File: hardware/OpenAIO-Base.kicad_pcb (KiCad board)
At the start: 8 copper layers, 35 x 35 mm, 264 parts, among them J15 5V, J16 5V, J17 GND, J18 GND, J20 LED, J21 LED, J24 5V, J25 5V, J27 GND, J28 GND, J29 BUZ-, J31 LED, J32 LED, J33 BUZ+, J41 10V, J51 GND, J90 OpenAIO-Core PCBA (consigned), Q10 DOY180N03T, Q11 DOY180N03T, Q12 DOY180N03T, Q13 DOY180N03T, Q14 DOY180N03T, Q15 DOY180N03T, Q16 DOY180N03T, Q17 DOY180N03T, Q18 DOY180N03T, Q19 DOY180N03T, Q20 DOY180N03T, Q21 DOY180N03T, Q22 DOY180N03T, Q23 DOY180N03T, Q24 DOY180N03T, Q25 DOY180N03T, Q26 DOY180N03T, Q3 DOY180N03T, Q4 DOY180N03T, Q5 DOY180N03T, Q6 DOY180N03T, Q7 DOY180N03T, Q8 DOY180N03T, Q9 DOY180N03T, U12 SM06B-SRSS-TB(LF)(SN), U13 AT32F421G8U7, U14 NSG2065Q, U15 AT32F421G8U7, U16 NSG2065Q, U17 AT32F421G8U7, U18 NSG2065Q, U19 AT32F421G8U7, U20 NSG2065Q, U21 SX1281IMLTRT, U22 ESP32-C3FH4, U23 TLV75533PDQNR, U24 AIO_outline, U25 INA186A3IDCKR, U27 TLV75533PDQNR, U3 LMR51430YFDDCR, U4 LMR51430YFDDCR, X2 CJ17-400001010B20

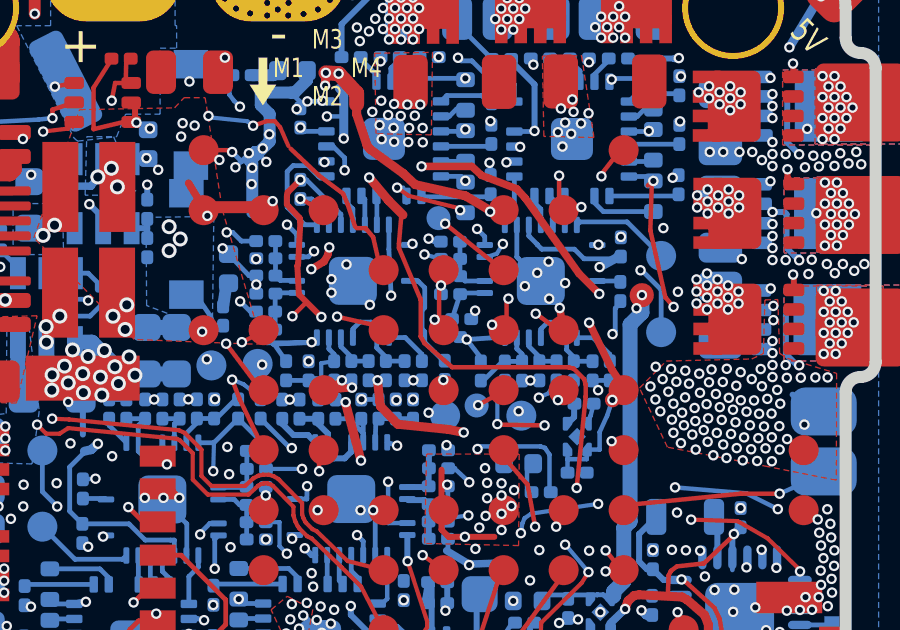
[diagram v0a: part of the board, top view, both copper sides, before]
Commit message: Base: revert the FB8e J90.14 GND via, R107 back to (78.73, 58.53) (FB7 step 4)
FB8e moved R107 (ESC4 phase-B divider) 0.37 mm east to make room for a
J90.14 GND via. That put R107.1 (/4B, the motor phase node) 0.045 mm from
the U19 QFN-28 body, beside U19's pin-8 terminal, which has no land: a
solder bridge there puts the phase voltage on the ESC4 MCU. The FB8e
classifier compared body-body and land-land only and missed the
land-to-body gap; the courtyard check found it. No other site for that via
(PB4 track, R105/R106 column, U19), so J90.14 goes back to its shared F
track via (78.41, 57.41). Geometry in the box equals b27fb75.
DRC 0 errors, unconnected 0, parity 70, +BATT 0.585 GND 0.357 mOhm,
+5V 56.4 mV.

Co-Authored-By: Claude Opus 5.5 <noreply@anthropic.com>
Claude-Session: https://claude.ai/code/session_01KTp3FLjVXfXdWrkmr6af7d
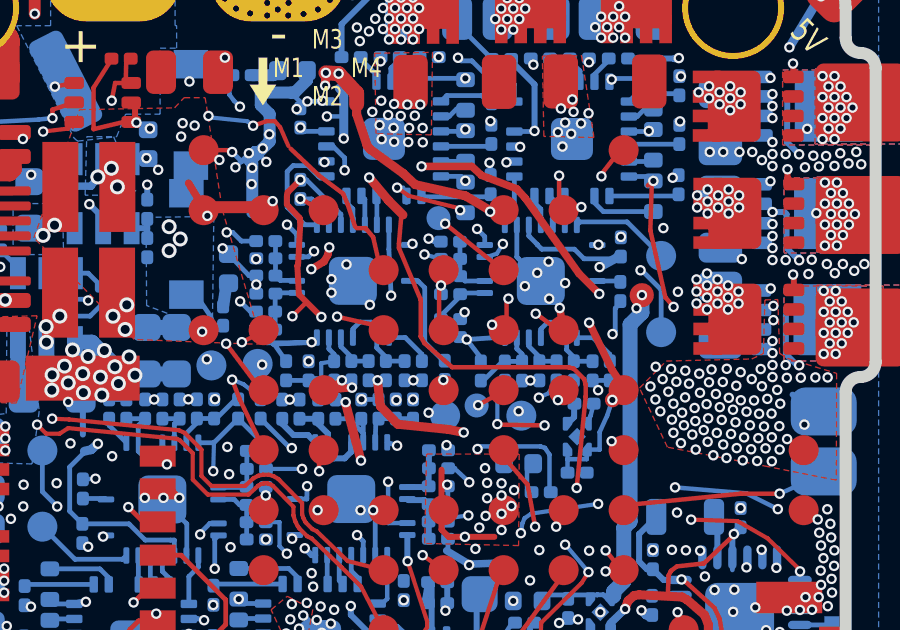
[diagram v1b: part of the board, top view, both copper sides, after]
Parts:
- moved R107 0.37 mm to (78.7, 58.5)
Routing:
- net GND: vias 592 -> 591
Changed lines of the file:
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@@
 	(footprint "Resistor_SMD:R_0201_0603Metric"
 		(layer "B.Cu")
-		(at 79.1 58.53 180)
+		(at 78.73 58.53 180)
 		(descr "Resistor SMD 0201 (0603 Metric), square (rectangular) end terminal, IPC-7351 nominal, (Body size source: https://www.vishay.com/docs/20052/crcw0201e3.pdf)")
 		(tags "resistor")
@@
 	)
 	(via
-		(at 78.2 58.55)
-		(size 0.35)
-		(drill 0.2)
-		(layers "F.Cu" "B.Cu")
-		(net "GND")
-	)
-	(via
 		(at 85.79 71.24)
 		(size 0.35)
@@
 	)
 	(via
-		(at 79.55 58.25)
-		(size 0.35)
-		(drill 0.2)
-		(layers "F.Cu" "B.Cu")
-		(net "/4B")
-	)
-	(via
 		(at 91.81 54.33)
 		(size 0.35)
@@
 	)
 	(via
+		(at 79.2 58.3)
+		(size 0.35)
+		(drill 0.2)
+		(layers "F.Cu" "B.Cu")
+		(net "/4B")
+	)
+	(via
 		(at 91.21 54.68)
 		(size 0.35)
@@
 	)
 	(segment
-		(start 79.42 58.53)
-		(end 79.55 58.25)
+		(start 79.05 58.4)
+		(end 79.2 58.3)
+		(width 0.16)
+		(layer "B.Cu")
+		(net "/4B")
+	)
+	(segment
+		(start 79.05 58.53)
+		(end 79.05 58.4)
 		(width 0.16)
 		(layer "B.Cu")
@@
 	)
 	(segment
-		(start 79.55 58.25)
+		(start 79.2 58.3)
 		(end 80.81 58.37)
 		(width 0.1)
@@
 	)
 	(segment
-		(start 78.78 58.53)
-		(end 78.41 59.13)
+		(start 79.162508 57.661096)
+		(end 79.870343 57.661096)
 		(width 0.16)
 		(layer "B.Cu")
@@
 	)
 	(segment
-		(start 79.162508 57.661096)
-		(end 79.870343 57.661096)
+		(start 79.1625 57.6611)
+		(end 78.41 58.4136)
 		(width 0.16)
 		(layer "B.Cu")
@@
 	)
 	(segment
-		(start 79.05 57.7)
-		(end 78.78 58.53)
+		(start 78.41 58.4136)
+		(end 78.41 59.13)
 		(width 0.16)
 		(layer "B.Cu")
@@
 	)
 	(segment
-		(start 77.78 58.86)
-		(end 77.87 58.95)
-		(width 0.16)
-		(layer "B.Cu")
-		(net "Net-(U17-PB4)")
-	)
-	(segment
 		(start 77.64199 57.256327)
 		(end 77.870279 57.484616)
@@
 	)
 	(segment
-		(start 77.87 57.485)
-		(end 77.87 58.15)
-		(width 0.16)
-		(layer "B.Cu")
-		(net "Net-(U17-PB4)")
-	)
-	(segment
-		(start 77.87 58.15)
-		(end 77.78 58.24)
+		(start 77.8703 57.4846)
+		(end 77.8703 59.3039)
 		(width 0.16)
 		(layer "B.Cu")
@@
 		(width 0.16)
 		(layer "B.Cu")
-		(net "Net-(U17-PB4)")
-	)
-	(segment
-		(start 77.87 58.95)
-		(end 77.87 59.304)
-		(width 0.16)
-		(layer "B.Cu")
-		(net "Net-(U17-PB4)")
-	)
-	(segment
-		(start 77.78 58.24)
-		(end 77.78 58.86)
-		(width 0.16)
-		(layer "B.Cu")
